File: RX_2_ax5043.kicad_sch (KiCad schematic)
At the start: 19 parts, among them P2 CONUFL001-SMD-T, Q4 DMP2037U-7, U15 AX5043

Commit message: Update schematics to match what is done to the boards so far
Get ready to split off a branch where the updates to the board can be
done while still keeping updates for the prototypes.

Signed-off-by: Corey Minyard <corey@minyard.net>
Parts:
- L6: value 0 -> 18hH 2%
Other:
- note removed: "Shorting jumper if no inductor"
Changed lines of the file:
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@@
 		)
 	)
-	(text "Shorting jumper\nif no inductor"
-		(exclude_from_sim no)
-		(at 195.58 177.165 0)
-		(effects
-			(font
-				(size 1.524 1.524)
-			)
-			(justify left bottom)
-		)
-	)
 	(text "RECEIVER 2"
 		(exclude_from_sim no)
@@
 			)
 		)
-		(property "Value" "0"
+		(property "Value" "18hH 2%"
 			(at 204.47 171.45 90)
 			(effects

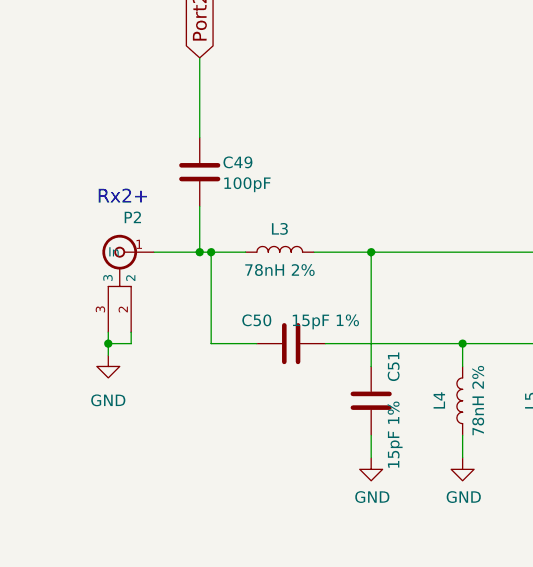
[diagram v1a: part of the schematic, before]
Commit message: Clean up the U.FL connectors a little more
Re-add the ones for TX/RX so both MMCX and U.FL are available.

Move P8 to a better location.

Signed-off-by: Corey Minyard <corey@minyard.net>
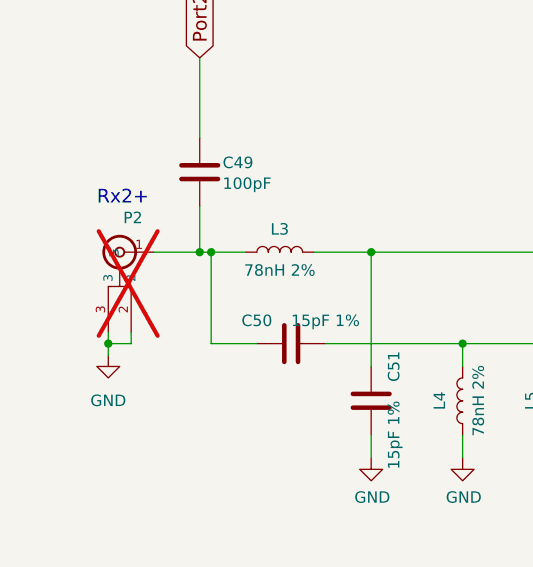
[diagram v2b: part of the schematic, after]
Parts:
- P2: now not fitted; now left out of the parts list
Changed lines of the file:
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@@
 		(unit 1)
 		(exclude_from_sim no)
-		(in_bom yes)
+		(in_bom no)
 		(on_board yes)
-		(dnp no)
+		(dnp yes)
 		(property "Reference" "P2"
 			(at 124.46 119.38 0)

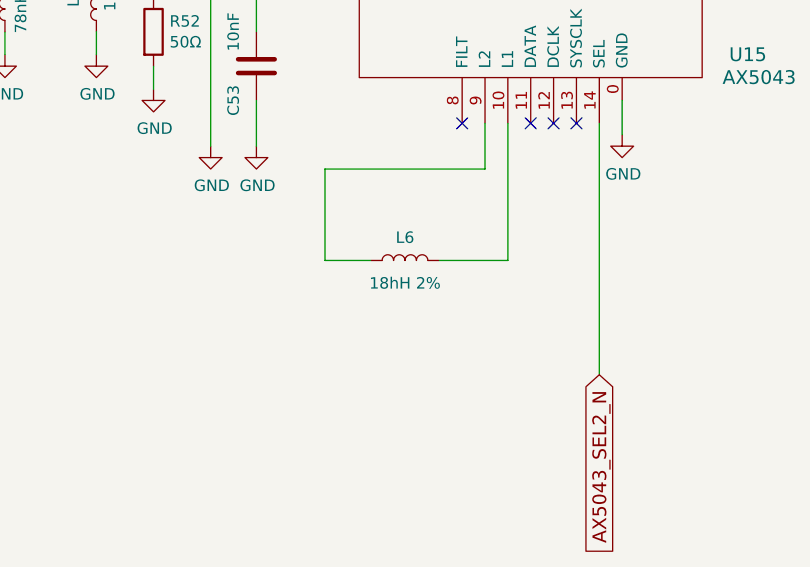
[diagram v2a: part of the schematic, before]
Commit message: Clean up BOM issues
Fix missing parts and mistypes parts.

Signed-off-by: Corey Minyard <corey@minyard.net>
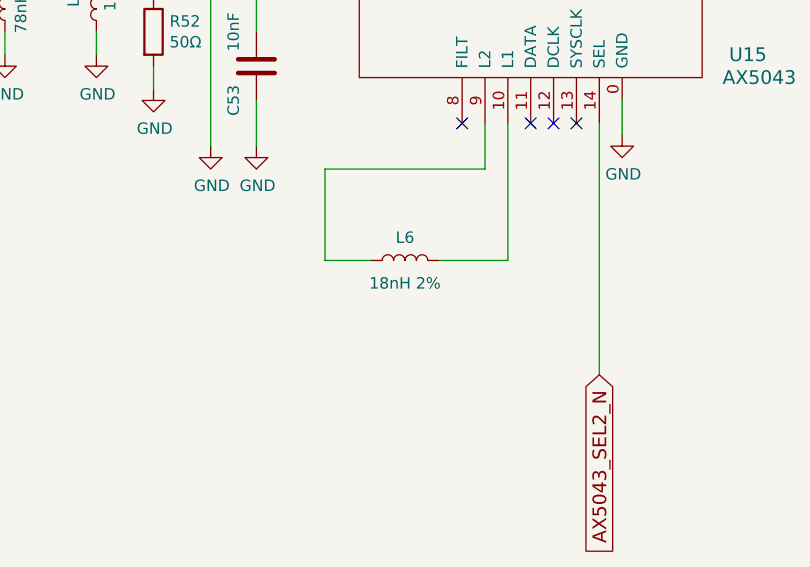
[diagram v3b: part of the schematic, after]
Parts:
- L6: value 18hH 2% -> 18nH 2%
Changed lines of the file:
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@@
 			)
 		)
-		(property "Value" "18hH 2%"
+		(property "Value" "18nH 2%"
 			(at 204.47 171.45 90)
 			(effects

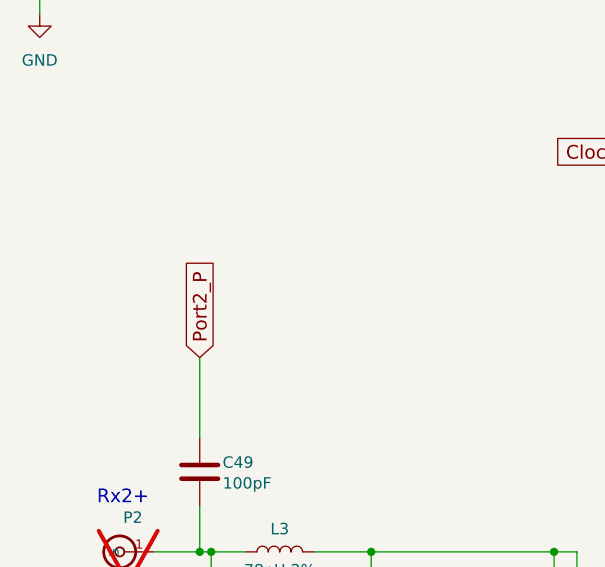
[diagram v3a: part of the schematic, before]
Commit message: Run the extra GPIOs to the PC104
They were recently freed with the ABF rework, use them.

Also, a kicad update broke some stuff, fix it.

Signed-off-by: Corey Minyard <corey@minyard.net>
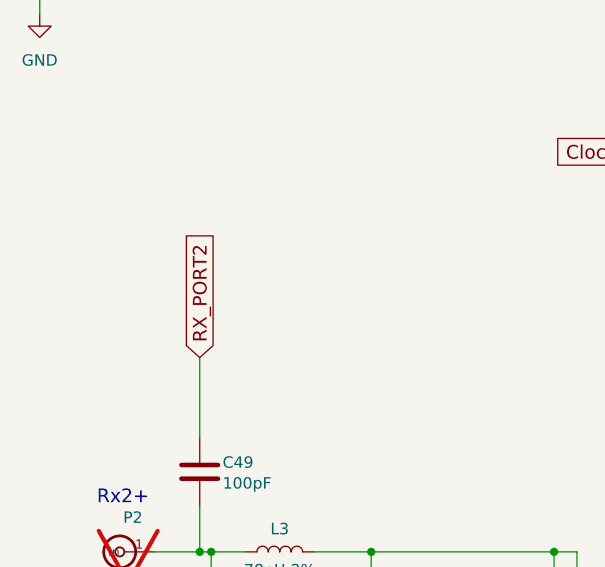
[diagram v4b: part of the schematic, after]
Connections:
- net Port2_P renamed RX_PORT2
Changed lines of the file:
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@@
 		)
 	)
-	(global_label "Port2_P"
+	(global_label "RX_PORT2"
 		(shape input)
 		(at 130.81 101.6 90)
@@
 		)
 		(property "Intersheetrefs" "${INTERSHEET_REFS}"
-			(at 130.81 89.9495 90)
+			(at 130.81 87.4096 90)
 			(effects
 				(font

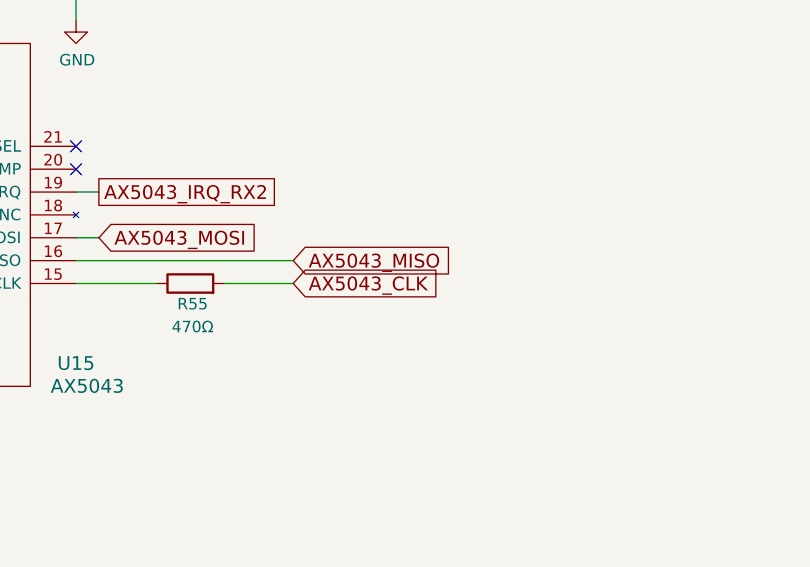
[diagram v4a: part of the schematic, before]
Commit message: Get the board ready for operation
Make the board ready as a final product, remove the lab testing portions
and add in the things required for full operation.

Signed-off-by: Corey Minyard <corey@minyard.net>
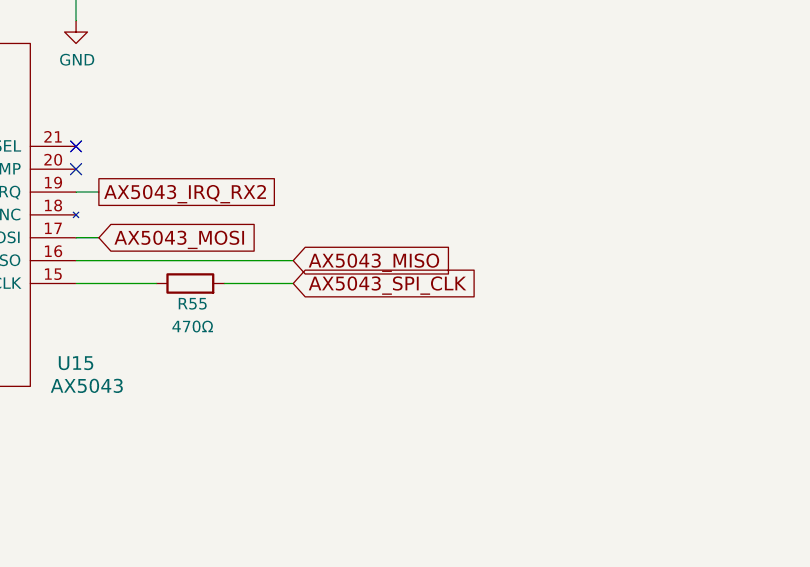
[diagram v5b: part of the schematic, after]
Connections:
- net AX5043_CLK renamed AX5043_SPI_CLK
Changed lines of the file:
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@@
 		)
 	)
-	(global_label "AX5043_CLK"
+	(global_label "AX5043_SPI_CLK"
 		(shape input)
 		(at 266.7 137.16 0)

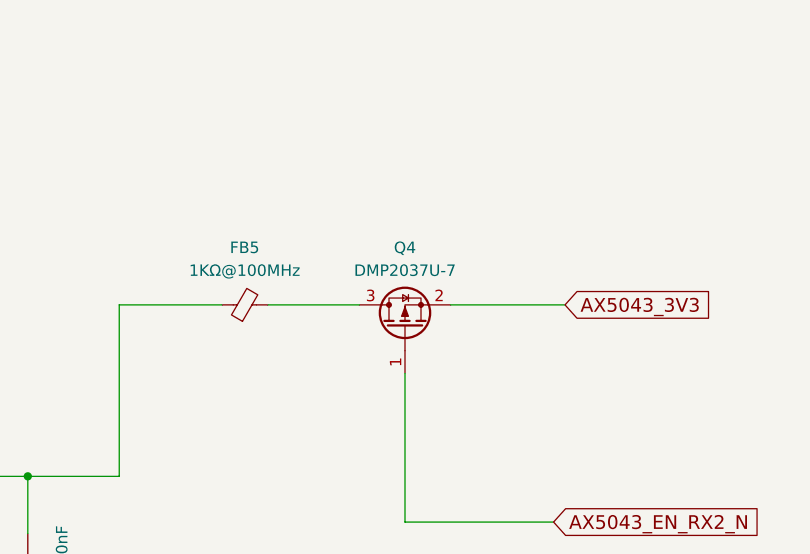
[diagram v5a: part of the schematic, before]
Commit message: Parts replacements for out of stock parts
Signed-off-by: Corey Minyard <corey@minyard.net>
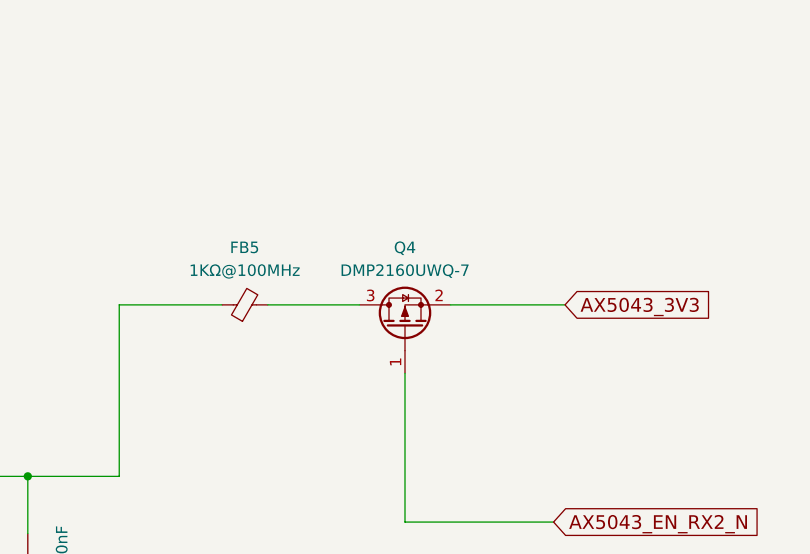
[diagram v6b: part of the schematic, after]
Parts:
- Q4: value DMP2037U-7 -> DMP2160UWQ-7; footprint Package_TO_SOT_SMD:SOT-23 -> Package_TO_SOT_SMD:SOT-323_SC-70
